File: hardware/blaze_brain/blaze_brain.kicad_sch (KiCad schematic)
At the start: 23 parts, among them J1 Conn_01x02, J3 Conn_01x30, J4 Micro_SD_Card, J5 Conn_01x03_Pin, Q2 FDN340P, U1 TCAN1044VDDFR, U3 Teensy4.0, U4 W25N02KVZEIR

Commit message: Brain Footprint Assignment
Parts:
- C1, C2, C3, C5, C6, C7: footprint (none) -> Capacitor_SMD:C_0603_1608Metric
- J3: footprint (none) -> Blaze_Library:HRS_DF17_1.0H_-30DP-0.5V_57_
- R1, R2, R3, R4, R5, R6: footprint (none) -> Resistor_SMD:R_0603_1608Metric
- U1: footprint (none) -> Package_SON:Texas_S-PVSON-N8
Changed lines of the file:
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@@
 			)
 		)
-		(property "Footprint" ""
+		(property "Footprint" "Resistor_SMD:R_0603_1608Metric"
 			(at 246.634 141.224 90)
 			(effects
@@
 			)
 		)
-		(property "Footprint" ""
+		(property "Footprint" "Resistor_SMD:R_0603_1608Metric"
 			(at 246.634 145.796 90)
 			(effects
@@
 			)
 		)
-		(property "Footprint" ""
+		(property "Footprint" "Capacitor_SMD:C_0603_1608Metric"
 			(at 179.3748 148.59 0)
 			(effects
@@
 			)
 		)
-		(property "Footprint" ""
+		(property "Footprint" "Capacitor_SMD:C_0603_1608Metric"
 			(at 32.7152 50.8 0)
 			(effects
@@
 			)
 		)
-		(property "Footprint" ""
+		(property "Footprint" "Capacitor_SMD:C_0603_1608Metric"
 			(at 186.3852 148.59 0)
 			(effects
@@
 			)
 		)
-		(property "Footprint" ""
+		(property "Footprint" "Resistor_SMD:R_0603_1608Metric"
 			(at 41.656 54.864 90)
 			(effects
@@
 			)
 		)
-		(property "Footprint" ""
+		(property "Footprint" "Package_SON:Texas_S-PVSON-N8"
 			(at 212.09 152.4 0)
 			(effects
@@
 			)
 		)
-		(property "Footprint" ""
+		(property "Footprint" "Resistor_SMD:R_0603_1608Metric"
 			(at 26.924 47.244 90)
 			(effects
@@
 			)
 		)
-		(property "Footprint" ""
+		(property "Footprint" "Capacitor_SMD:C_0603_1608Metric"
 			(at 42.8752 106.68 0)
 			(effects
@@
 			)
 		)
-		(property "Footprint" ""
+		(property "Footprint" "Blaze_Library:HRS_DF17_1.0H_-30DP-0.5V_57_"
 			(at 273.05 67.31 0)
 			(effects
@@
 			)
 		)
-		(property "Footprint" ""
+		(property "Footprint" "Resistor_SMD:R_0603_1608Metric"
 			(at 167.894 106.934 90)
 			(effects
@@
 			)
 		)
-		(property "Footprint" ""
+		(property "Footprint" "Capacitor_SMD:C_0603_1608Metric"
 			(at 41.6052 161.29 0)
 			(effects
@@
 			)
 		)
-		(property "Footprint" ""
+		(property "Footprint" "Capacitor_SMD:C_0603_1608Metric"
 			(at 255.27 143.51 0)
 			(effects
@@
 			)
 		)
-		(property "Footprint" ""
+		(property "Footprint" "Resistor_SMD:R_0603_1608Metric"
 			(at 228.854 151.384 90)
 			(effects

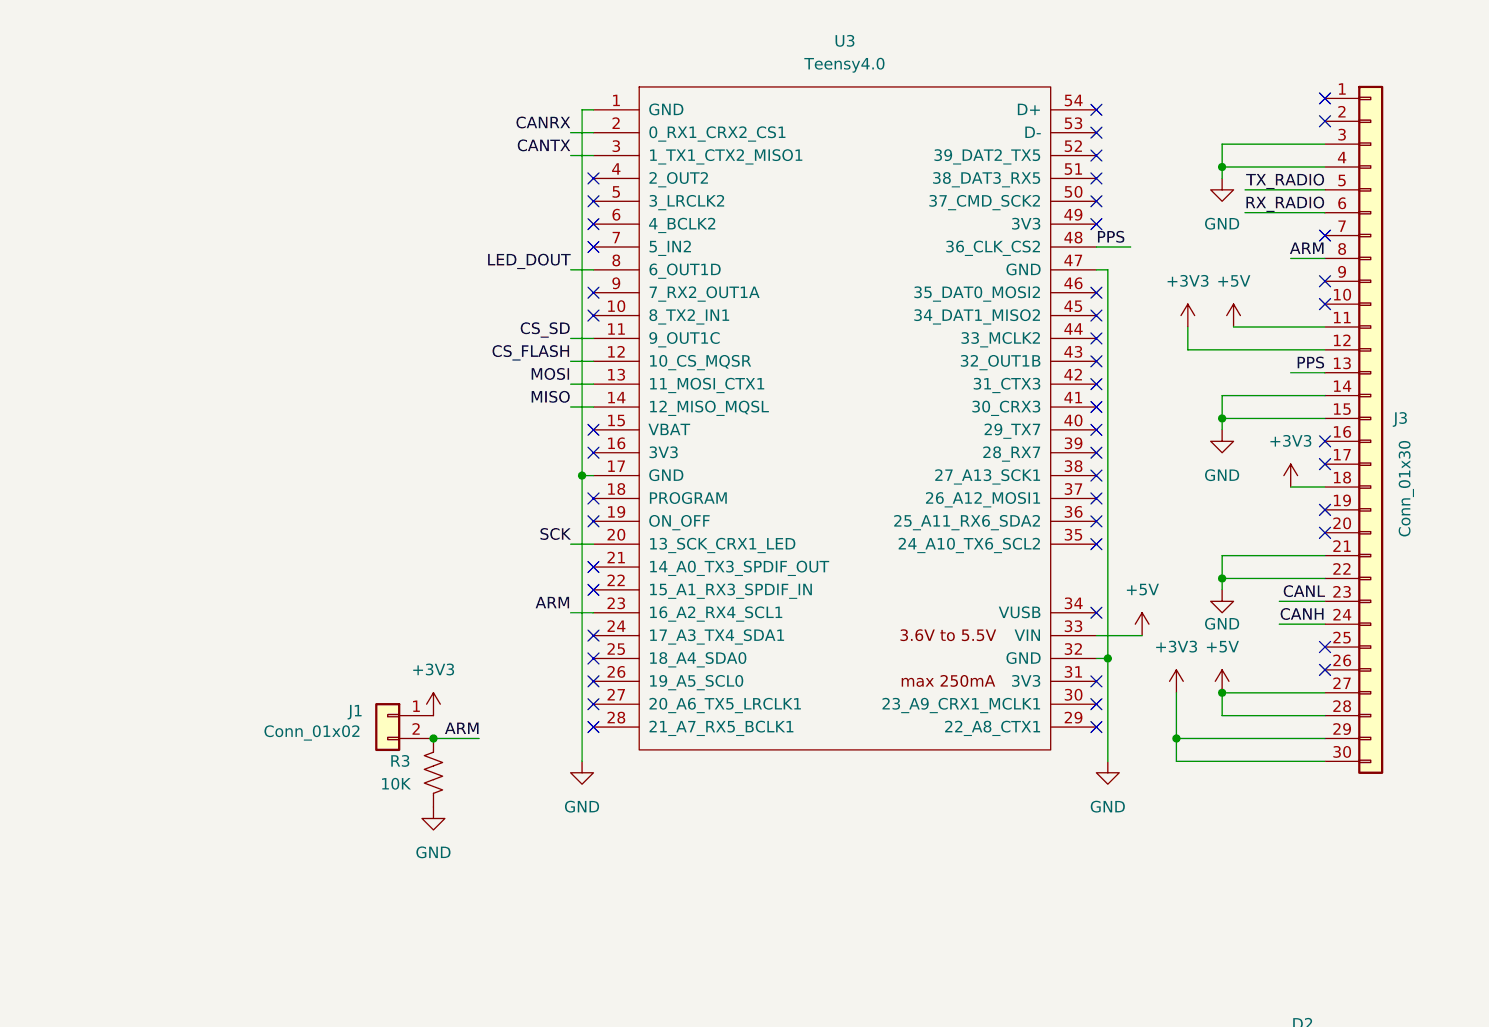
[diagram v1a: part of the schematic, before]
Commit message: Added mirror interconnect and PCB to brain
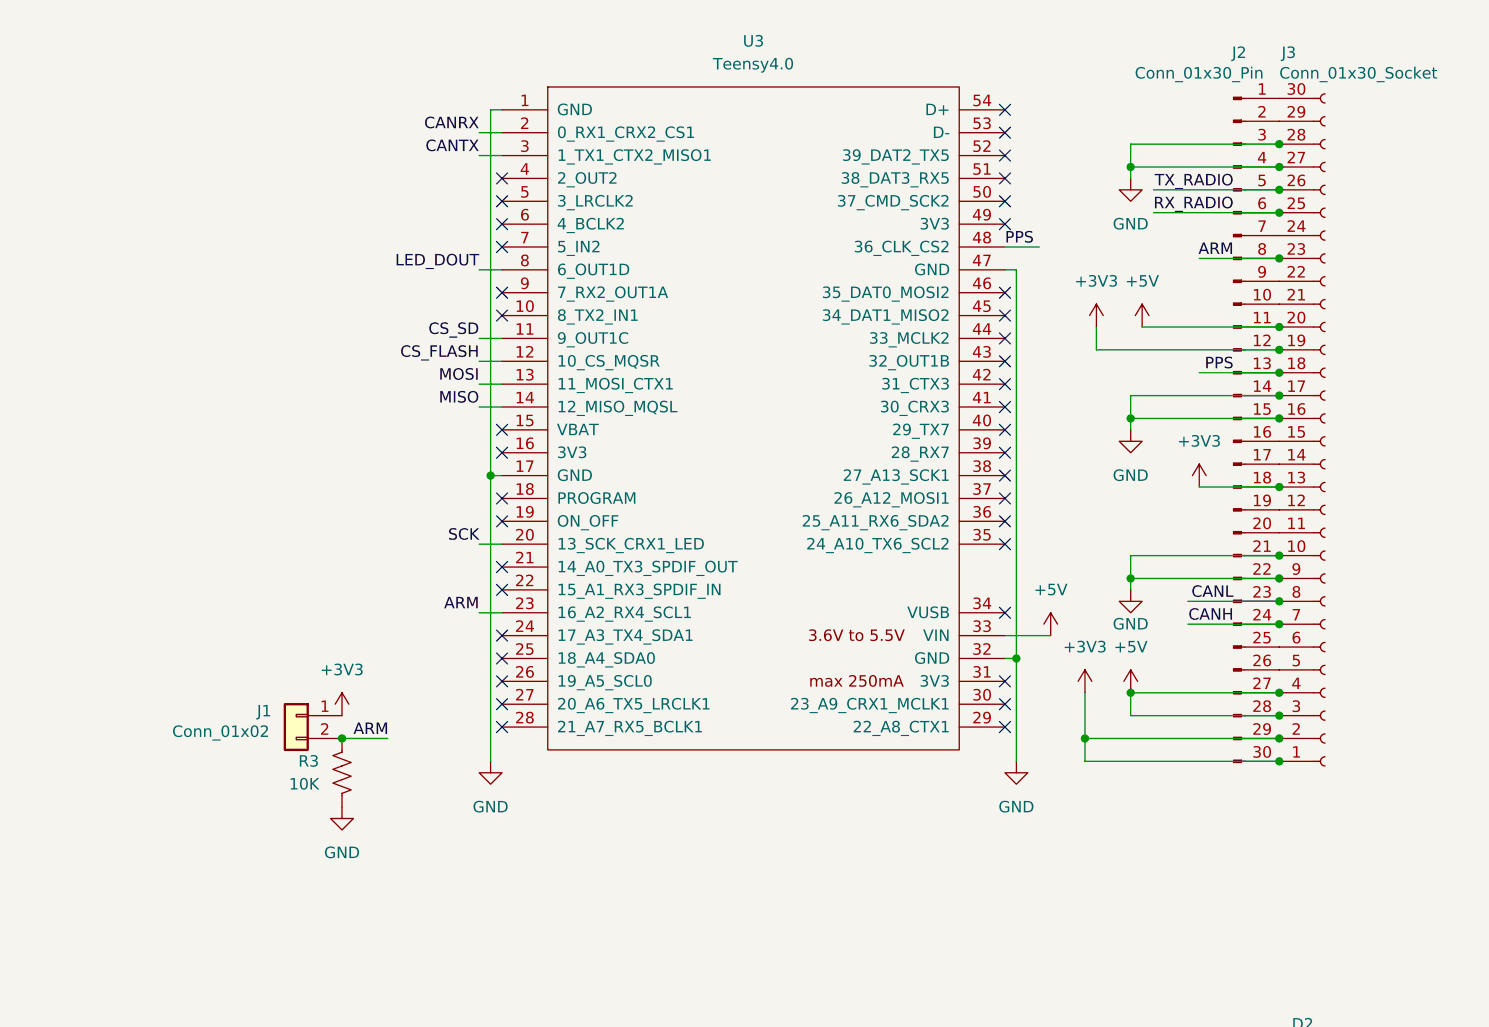
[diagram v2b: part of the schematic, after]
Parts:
- removed J3: Conn_01x30, Blaze_Library:HRS_DF17_1.0H_-30DP-0.5V_57_, symbol Connector_Generic:Conn_01x30
- added J2: Conn_01x30_Pin, Blaze_Library:HRS_DF17_1.0H_-30DP-0.5V_57_, symbol Connector:Conn_01x30_Pin
- added J3: Conn_01x30_Socket, Blaze_Library:HRS_DF17_1.0H_-30DP-0.5V_57_, symbol Connector:Conn_01x30_Socket
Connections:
- net +3V3: now also J2.12 (Pin_12), J2.18 (Pin_18), J2.29 (Pin_29), J2.30 (Pin_30), J3.1 (Pin_1), J3.13 (Pin_13), J3.19 (Pin_19), J3.2 (Pin_2)
- net +5V: now also J2.11 (Pin_11), J2.27 (Pin_27), J2.28 (Pin_28), J3.20 (Pin_20), J3.3 (Pin_3), J3.4 (Pin_4)
- net ARM: now also J2.8 (Pin_8), J3.23 (Pin_23)
- net CANH: now also J2.24 (Pin_24), J3.7 (Pin_7)
- net CANL: now also J2.23 (Pin_23), J3.8 (Pin_8)
- net GND: now also J2.14 (Pin_14), J2.15 (Pin_15), J2.21 (Pin_21), J2.22 (Pin_22), J2.3 (Pin_3), J2.4 (Pin_4), J3.10 (Pin_10), J3.16 (Pin_16), J3.17 (Pin_17), J3.27 (Pin_27), J3.28 (Pin_28), J3.9 (Pin_9)
- net PPS: now also J2.13 (Pin_13), J3.18 (Pin_18)
- net RX_RADIO: now also J2.6 (Pin_6), J3.25 (Pin_25)
- net TX_RADIO: now also J2.5 (Pin_5), J3.26 (Pin_26)
- new net: J2.20 (Pin_20), J3.11 (Pin_11)
- new net: J2.19 (Pin_19), J3.12 (Pin_12)
- new net: J2.17 (Pin_17), J3.14 (Pin_14)
- new net: J2.16 (Pin_16), J3.15 (Pin_15)
- new net: J2.10 (Pin_10), J3.21 (Pin_21)
- new net: J2.9 (Pin_9), J3.22 (Pin_22)
- new net: J2.7 (Pin_7), J3.24 (Pin_24)
- new net: J2.2 (Pin_2), J3.29 (Pin_29)
- new net: J2.1 (Pin_1), J3.30 (Pin_30)
- new net: J2.26 (Pin_26), J3.5 (Pin_5)
- new net: J2.25 (Pin_25), J3.6 (Pin_6)
- no-connect marks 54 -> 43
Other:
- moved on the sheet: J1, R3, U3

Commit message: Added footprints
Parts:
- J1: footprint (none) -> Connector_PinHeader_2.54mm:PinHeader_1x01_P2.54mm_Vertical
- J4: footprint (none) -> Blaze_Library:CONN_47219-2001_MOL
- J5: footprint (none) -> Connector_PinHeader_2.54mm:PinHeader_1x03_P2.54mm_Vertical
- U3: footprint (none) -> Blaze_Library:Teensy40
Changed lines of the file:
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@@
 			)
 		)
-		(property "Footprint" ""
+		(property "Footprint" "Blaze_Library:CONN_47219-2001_MOL"
 			(at 106.68 35.56 0)
 			(effects
@@
 			)
 		)
-		(property "Footprint" ""
+		(property "Footprint" "Blaze_Library:Teensy40"
 			(at 194.31 62.23 0)
 			(effects
@@
 			)
 		)
-		(property "Footprint" ""
+		(property "Footprint" "Connector_PinHeader_2.54mm:PinHeader_1x03_P2.54mm_Vertical"
 			(at 88.9 157.48 0)
 			(effects
@@
 			)
 		)
-		(property "Footprint" ""
+		(property "Footprint" "Connector_PinHeader_2.54mm:PinHeader_1x01_P2.54mm_Vertical"
 			(at 153.67 100.33 0)
 			(effects

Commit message: Connected radio UART
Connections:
- net RX_RADIO: now also U3.10 (8_TX2_IN1)
- net TX_RADIO: now also U3.9 (7_RX2_OUT1A)
- no-connect marks 43 -> 41
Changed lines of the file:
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@@
-	)
-	(no_connect
-		(at 176.53 53.34)
 	)
 	(no_connect
@@
 	)
 	(no_connect
-		(at 176.53 55.88)
-	)
-	(no_connect
 		(at 176.53 76.2)
 	)
@@
 		(pts
 			(xy 52.07 50.8) (xy 54.61 50.8)
+		)
+		(stroke
+			(width 0)
+			(type default)
+		)
+	)
+	(wire
+		(pts
+			(xy 173.99 55.88) (xy 176.53 55.88)
+		)
+		(stroke
+			(width 0)
+			(type default)
+		)
+	)
+	(wire
+		(pts
+			(xy 173.99 53.34) (xy 176.53 53.34)
 		)
 		(stroke
@@
 		)
 	)
+	(label "TX_RADIO"
+		(at 173.99 53.34 180)
+		(fields_autoplaced yes)
+		(effects
+			(font
+				(size 1.27 1.27)
+			)
+			(justify right bottom)
+		)
+	)
 	(label "MOSI"
 		(at 52.07 40.64 180)
@@
 		(fields_autoplaced yes)
 		(effects
+			(font
+				(size 1.27 1.27)
+			)
+			(justify right bottom)
+		)
+	)
+	(label "RX_RADIO"
+		(at 173.99 55.88 180)
+		(fields_autoplaced yes)
+		(effects

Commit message: Routed board
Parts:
- removed J2: Conn_01x30_Pin, Blaze_Library:HRS_DF17_1.0H_-30DP-0.5V_57_, symbol Connector:Conn_01x30_Pin
- removed J3: Conn_01x30_Socket, Blaze_Library:HRS_DF17_1.0H_-30DP-0.5V_57_, symbol Connector:Conn_01x30_Socket
- added J1: FrontInterconnect, Blaze_Library:HRS_DF17_1.0H_-30DP-0.5V_57_, symbol Blaze_Lib:DF17U-30_Male
- added J2: RearInterconnect, Blaze_Library:HRS_DF17_1.0H_-30DP-0.5V_57_, symbol Blaze_Lib:DF17U-30_Female
- renumbered C5 to C4, C7 to C5, D2 to D1, D1 to D2, J4 to J3, J1 to J4, Q2 to Q1, R4 to R1, R5 to R2, R6 to R3, R1 to R4, R2 to R5, R3 to R6, U3 to U2, U4 to U3
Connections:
- net +3V3: now also J1.10 (Pin_10), J1.16 (Pin_16), J1.27 (Pin_27), J1.28 (Pin_28), J2.15 (Pin_15), J2.21 (Pin_21), J2.3 (Pin_3), J2.4 (Pin_4)
- net +5V: now also J1.25 (Pin_25), J1.26 (Pin_26), J1.9 (Pin_9), J2.22 (Pin_22), J2.5 (Pin_5), J2.6 (Pin_6)
- net ARM: now also J1.6 (Pin_6), J2.25 (Pin_25)
- net CANH: now also J1.21 (Pin_21), J2.10 (Pin_10)
- net CANL: now also J1.22 (Pin_22), J2.9 (Pin_9)
- net GND: now also J1.1 (Pin_1), J1.12 (Pin_12), J1.13 (Pin_13), J1.19 (Pin_19), J1.2 (Pin_2), J1.20 (Pin_20), J1.S1 (Tab_1), J1.S2 (Tab_2), J2.11 (Pin_11), J2.12 (Pin_12), J2.18 (Pin_18), J2.19 (Pin_19), J2.29 (Pin_29), J2.30 (Pin_30), J2.S1 (Tab_1), J2.S2 (Tab_2)
- net PPS: now also J1.11 (Pin_11), J2.20 (Pin_20)
- net RX_RADIO: now also J1.3 (Pin_3), J2.28 (Pin_28)
- net TX_RADIO: now also J1.4 (Pin_4), J2.27 (Pin_27)
- new net: J1.14 (Pin_14), J2.17 (Pin_17)
- new net: J1.15 (Pin_15), J2.16 (Pin_16)
- new net: J1.17 (Pin_17), J2.14 (Pin_14)
- new net: J1.18 (Pin_18), J2.13 (Pin_13)
- new net: J1.23 (Pin_23), J2.8 (Pin_8)
- new net: J1.24 (Pin_24), J2.7 (Pin_7)
- new net: J1.29 (Pin_29), J2.2 (Pin_2)
- new net: J1.30 (Pin_30), J2.1 (Pin_1)
- new net: J1.5 (Pin_5), J2.26 (Pin_26)
- new net: J1.7 (Pin_7), J2.24 (Pin_24)
- new net: J1.8 (Pin_8), J2.23 (Pin_23)
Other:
- moved on the sheet: C4, C5, C6, D2, J3, J4, J5, Q1, R4, R5, R6, U2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

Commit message: Updated routing, rounded tracks
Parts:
- J4: footprint Connector_PinHeader_2.54mm:PinHeader_1x01_P2.54mm_Vertical -> Connector_PinHeader_2.54mm:PinHeader_1x02_P2.54mm_Horizontal
- J5: footprint Connector_PinHeader_2.54mm:PinHeader_1x03_P2.54mm_Vertical -> Connector_PinHeader_2.54mm:PinHeader_1x03_P2.54mm_Horizontal
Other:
- moved on the sheet: C4, C5, C6, D2, J3, J4, J5, Q1, R4, R5, R6, U2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
